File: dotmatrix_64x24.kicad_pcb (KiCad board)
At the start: 2 copper layers, 180 x 100 mm, 452 parts, among them CON1 BARREL_JACK, P1 CONN_01X09, P2 CONN_01X09, P3 CONN_01X04, P4 CONN_01X03, P5 USB_OTG, P6 CONN_01X03, Q1 NJL7302L-F3, Q2 Q_PNP_BEC 2SA1162, Q3 Q_NPN_BCE RN5006, SW1 SW_PUSH_SMALL_H, SW2 SW_PUSH_SMALL_H, SW3 SW_PUSH_SMALL_H, SW4 SW_PUSH_SMALL_H, SW5 SW_PUSH_SMALL_H, SW6 SW_PUSH_SMALL_H, SW7 SW_PUSH_SMALL_H, SW8 SW_PUSH_SMALL_H, U1 WROOM-02, U10 LED1642GW, U11 LED1642GW, U12 AE-BME280, U13 OKL-T/6-W5, U14 NJU7223, U15 DS1307, U16 CH340G, U17 OSRB38C9AA, U2 74HC595-alt-vdd, U3 TD62783, U4 74HC595-alt-vdd, U5 TD62783, U6 LED1642GW, U7 74HC595-alt-vdd, U8 TD62783, U9 LED1642GW, X1 CRYSTAL_SMD, Y1 12MHz

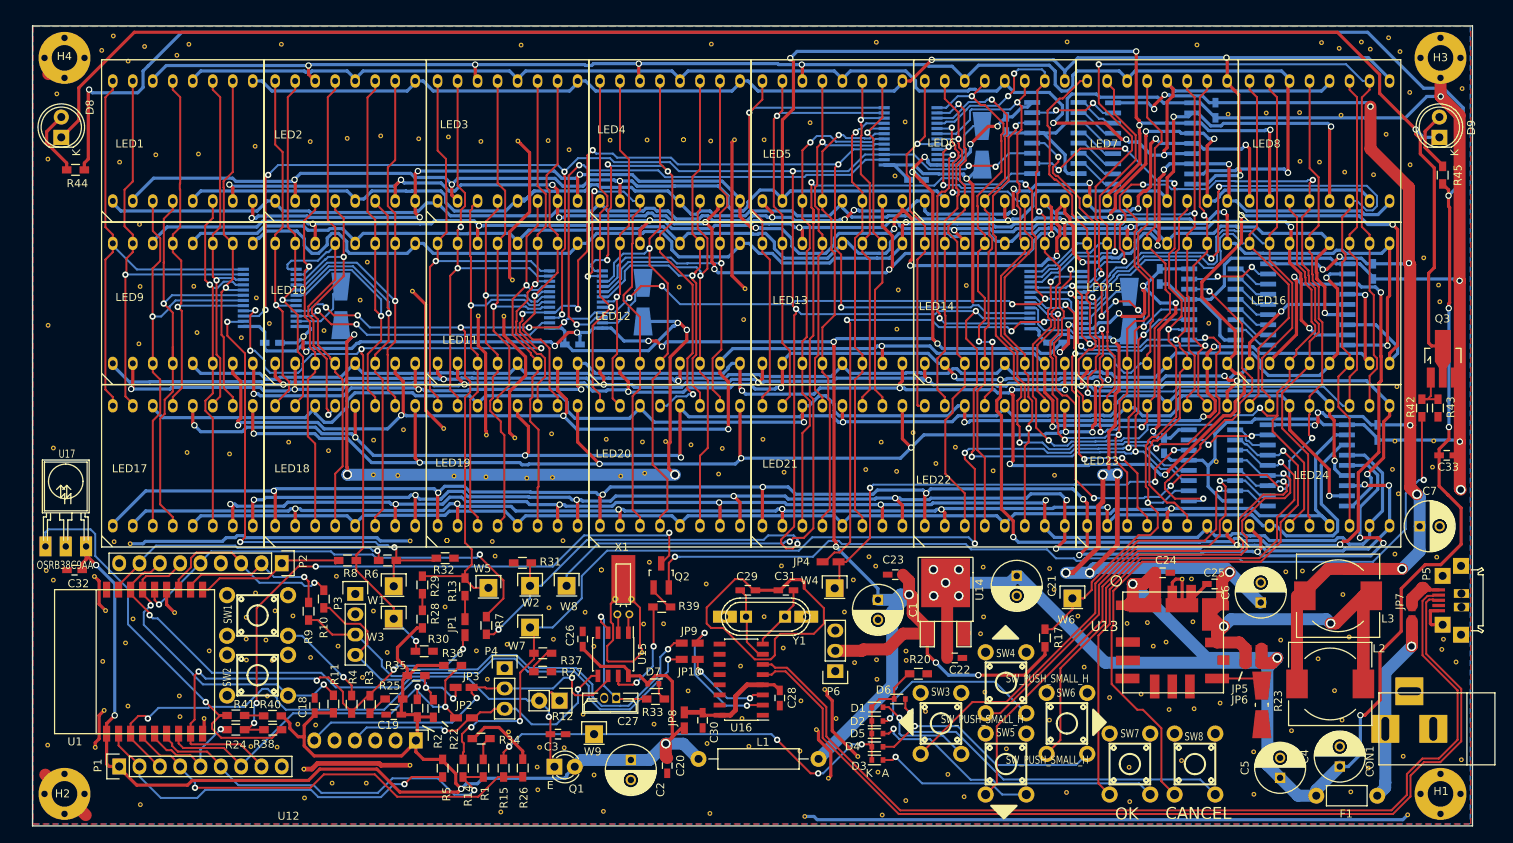
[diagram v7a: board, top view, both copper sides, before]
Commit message: Separated sensors/IR/RTC schematic sheet and improved IR transistor drive circuit
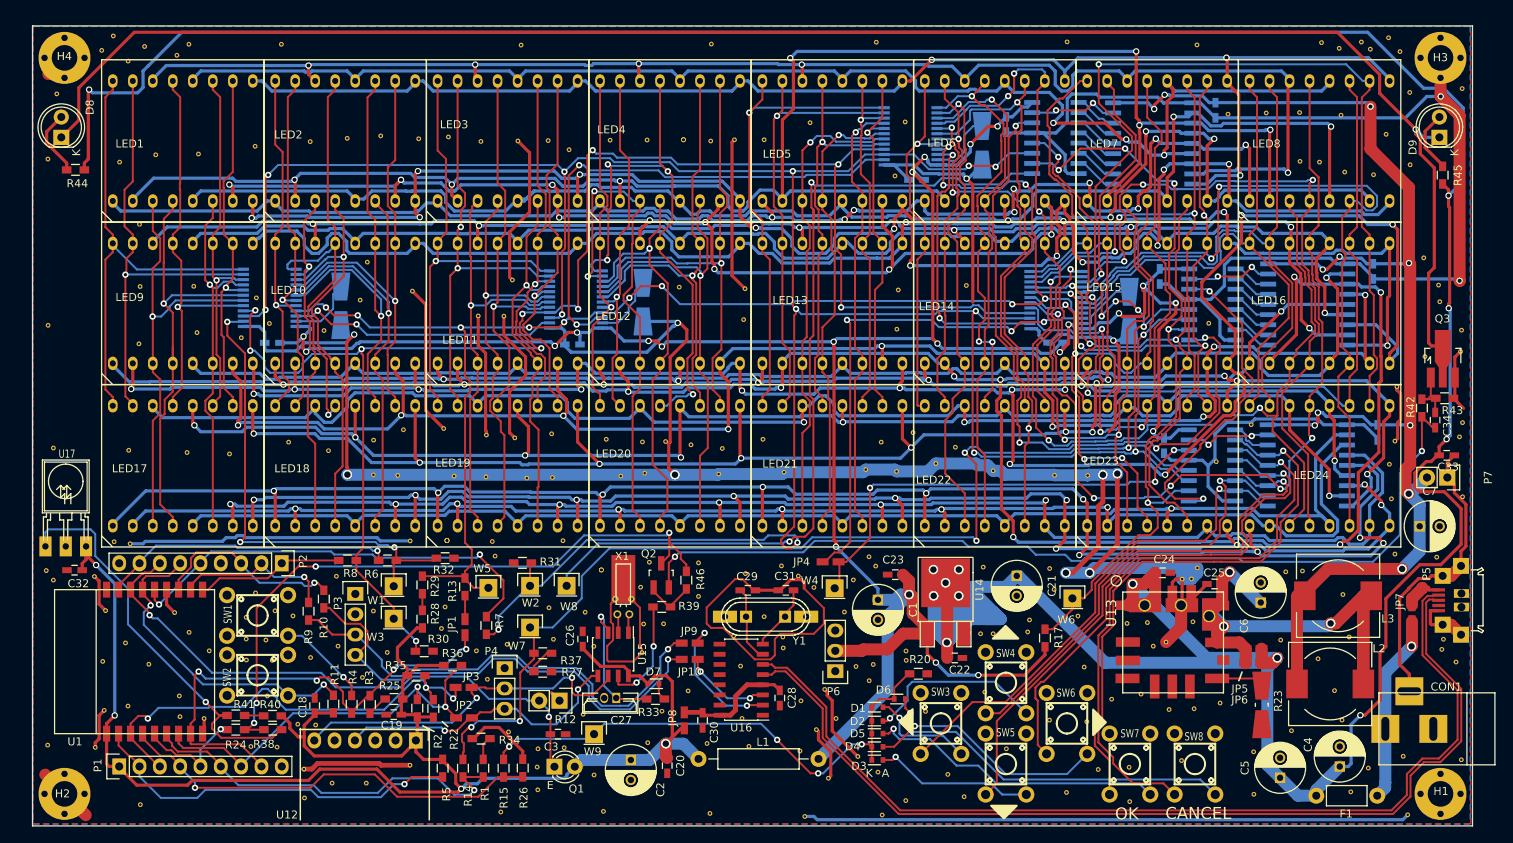
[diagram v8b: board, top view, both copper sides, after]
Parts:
- removed the REF** at (187.1, 63.9)
- added C34: 220p, Capacitors_SMD:C_0603_HandSoldering, F.Cu at (187.3, 61.3)
- added P7: CONN_01X02, Pin_Headers:Pin_Header_Straight_1x02, F.Cu at (188.8, 68.5)
- added R46: 10k, Resistors_SMD:R_0603_HandSoldering, F.Cu at (93.7, 81.3)
- added REF**: stitch-via-0.6mm, components:stitch-via-0.6mm, F.Cu at (88.9, 101.6)
- added REF**: stitch-via-0.6mm, components:stitch-via-0.6mm, F.Cu at (190.4, 63.4)
- added REF**: stitch-via-0.6mm, components:stitch-via-0.6mm, F.Cu at (24.0, 65.0)
- added REF**: stitch-via-0.6mm, components:stitch-via-0.6mm, F.Cu at (31.6, 87.8)
- added REF**: stitch-via-0.6mm, components:stitch-via-0.6mm, F.Cu at (63.1, 87.3)
- added REF**: stitch-via-0.6mm, components:stitch-via-0.6mm, F.Cu at (105.8, 88.4)
- added REF**: stitch-via-0.6mm, components:stitch-via-0.6mm, F.Cu at (99.6, 88.3)
- added REF**: stitch-via-0.6mm, components:stitch-via-0.6mm, F.Cu at (107.7, 80.8)
- added REF**: stitch-via-0.6mm, components:stitch-via-0.6mm, F.Cu at (101.1, 80.5)
- added REF**: stitch-via-0.6mm, components:stitch-via-0.6mm, F.Cu at (95.2, 79.1)
- added REF**: stitch-via-0.6mm, components:stitch-via-0.6mm, F.Cu at (109.7, 82.2)
- added REF**: stitch-via-0.6mm, components:stitch-via-0.6mm, F.Cu at (157.6, 79.8)
- added REF**: stitch-via-0.6mm, components:stitch-via-0.6mm, F.Cu at (136.4, 87.8)
- added REF**: stitch-via-0.6mm, components:stitch-via-0.6mm, F.Cu at (136.6, 86.3)
- added REF**: stitch-via-0.6mm, components:stitch-via-0.6mm, F.Cu at (145.2, 105.0)
- added REF**: stitch-via-0.6mm, components:stitch-via-0.6mm, F.Cu at (143.8, 99.0)
- added REF**: stitch-via-0.6mm, components:stitch-via-0.6mm, F.Cu at (143.9, 68.2)
- added REF**: stitch-via-0.6mm, components:stitch-via-0.6mm, F.Cu at (164.3, 61.8)
- added REF**: stitch-via-0.6mm, components:stitch-via-0.6mm, F.Cu at (186.1, 53.3)
- added REF**: stitch-via-0.6mm, components:stitch-via-0.6mm, F.Cu at (190.6, 50.0)
- added REF**: stitch-via-0.6mm, components:stitch-via-0.6mm, F.Cu at (190.5, 52.7)
- added REF**: stitch-via-0.6mm, components:stitch-via-0.6mm, F.Cu at (88.0, 82.2)
- added REF**: stitch-via-0.6mm, components:stitch-via-0.6mm, F.Cu at (190.8, 70.9)
- moved REF** 6.71 mm to (190.8, 61.6)
- moved REF** 6.00 mm to (26.5, 91.8)
- moved REF** 2.42 mm to (132.1, 88.0)
- moved REF** 1.90 mm to (90.7, 97.7)
- moved REF** 1.83 mm to (95.2, 83.3)
- moved R43 1.48 mm to (188.5, 58.5), turned to 180 degrees
- moved REF** 1.07 mm to (181.9, 71.1)
- moved REF** 0.98 mm to (116.6, 93.9)
- moved REF** 0.74 mm to (181.6, 66.8)
- moved REF** 0.71 mm to (117.1, 91.8)
- moved REF** 0.51 mm to (114.9, 92.1)
- moved REF** 0.33 mm to (146.9, 96.2)
- moved REF** 0.27 mm to (75.2, 102.4)
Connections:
- net /#IR_LED_EN renamed /IR_Sensor_RTC/#IR_LED_EN
- net /IR_LED_DRIVE renamed /IR_Sensor_RTC/IR_LED_DRIVE
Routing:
- net GND: track 776.0 -> 901.8 mm, vias 11 -> 12
- net VCC: track 440.9 -> 514.4 mm, vias 12 -> 13
- net Net-(C25-Pad1): track 116.5 -> 67.2 mm, vias 7 -> 3
- net /IR: track 78.2 -> 83.9 mm
- net /Sheet57A04605/SEL6: track 72.7 -> 75.9 mm
- net Net-(Q2-Pad1): track 3.42 -> 6.49 mm
- net Net-(C34-Pad1): track 5.59 -> 7.40 mm
- net /Sheet57A04605/r19: track 186.1 -> 184.4 mm
- net Net-(C34-Pad2): track 114.8 -> 116.4 mm
- net /Sheet57A04605/COLCLK: track 339.0 -> 337.4 mm
- net /Sheet57A04605/SEL4: track 64.4 -> 65.7 mm
- net /Sheet57A04605/LEDVDD: track 175.5 -> 174.3 mm
- net /Sheet57A04605/BUTTONSENSE: track 65.4 -> 66.5 mm
- net Net-(D4-Pad2): track 29.4 -> 30.3 mm
